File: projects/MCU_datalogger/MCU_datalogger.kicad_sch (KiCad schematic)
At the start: 25 parts, among them U1 24LC1025, U2 DS1337S_, U3 24LC1025, U4 ATMEGA328P-AU, Y1 32.768KHz, Y2 16MHz

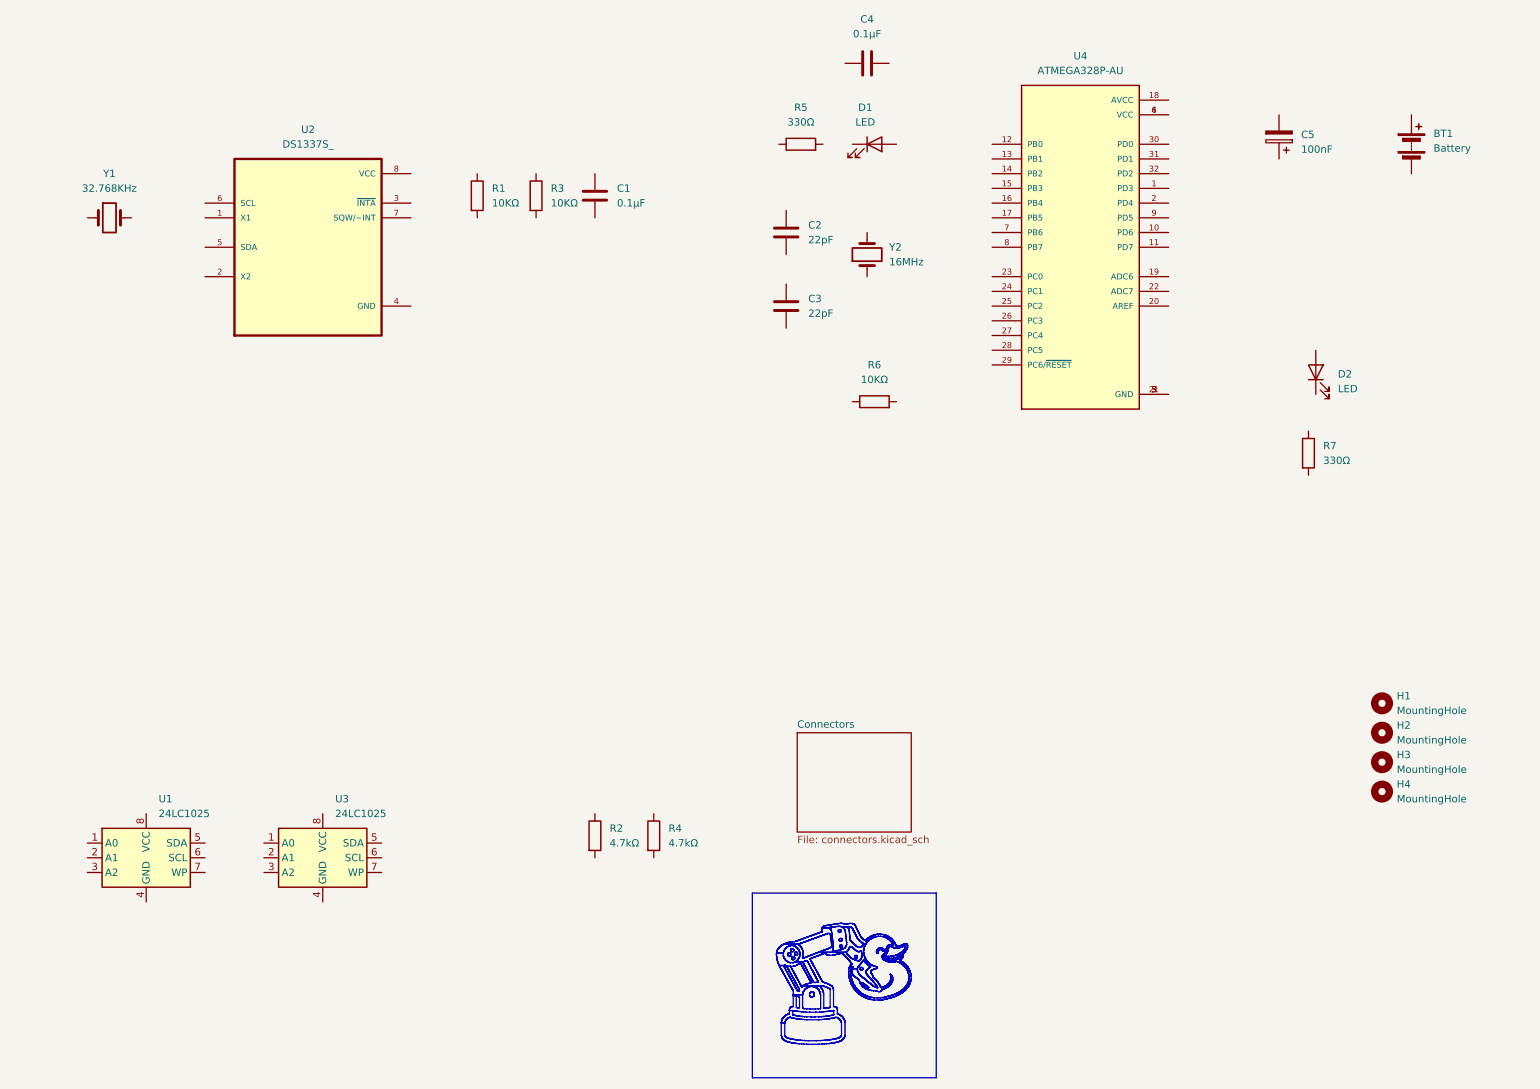
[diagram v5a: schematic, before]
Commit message: MCU datalogger - wiring of main sheet
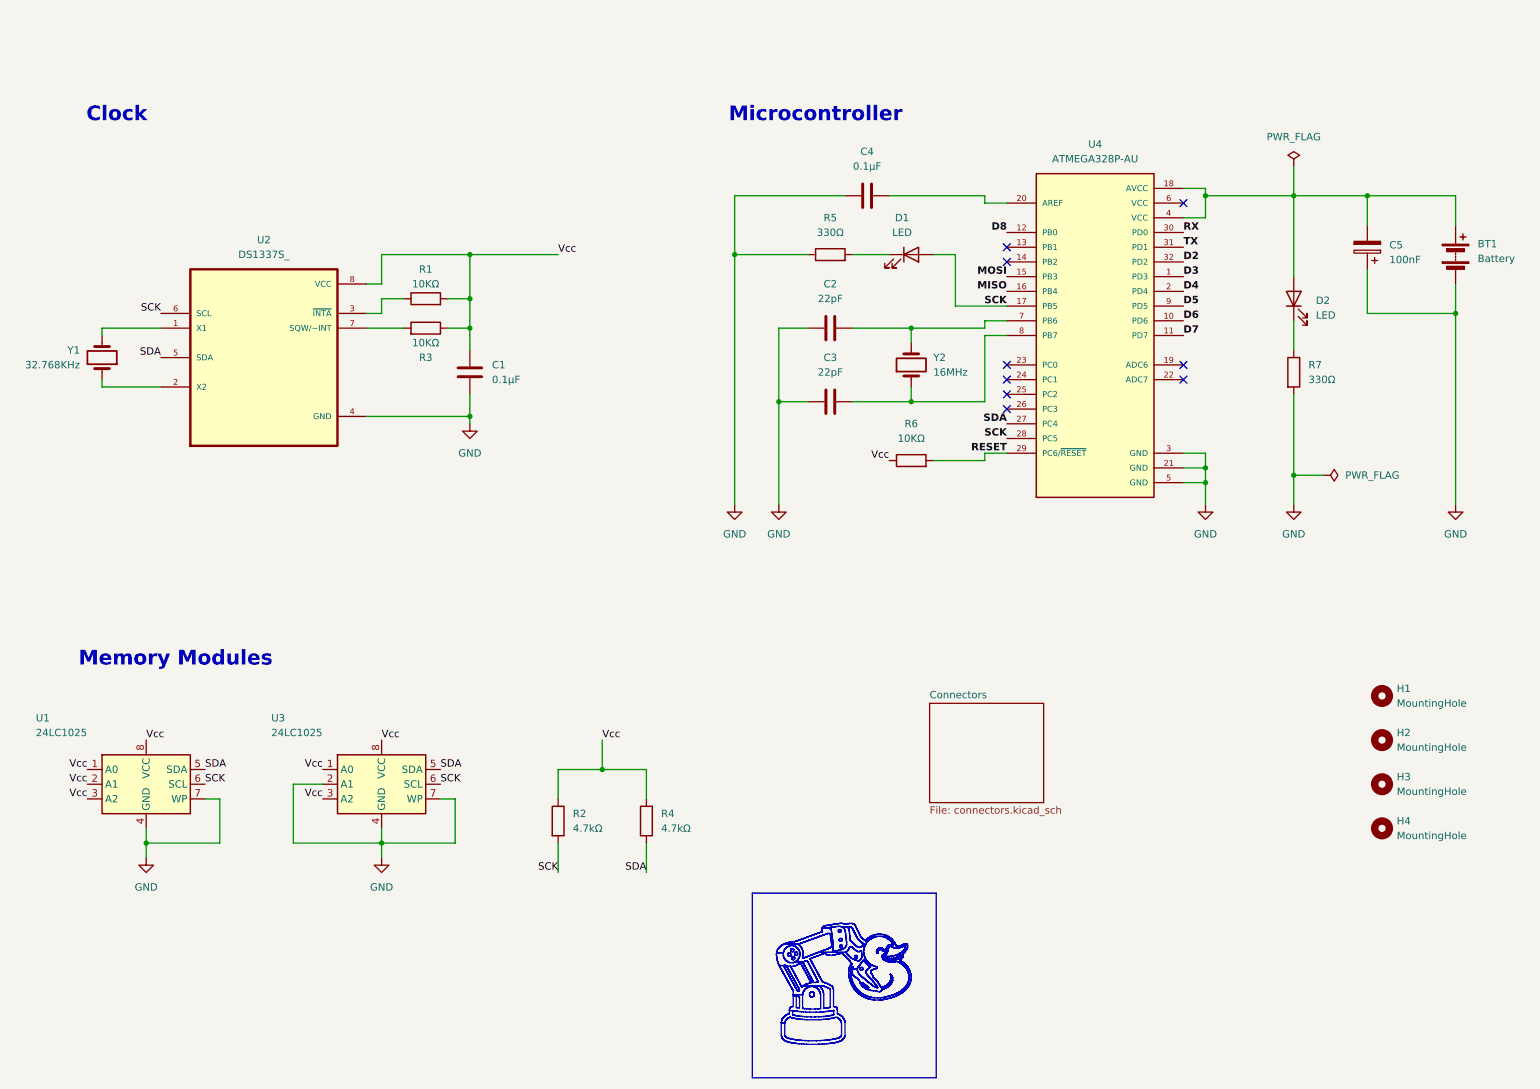
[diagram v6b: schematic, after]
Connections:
- net GND: now reaches C3.1
- net GND: now also BT1.2 (-), C1.2, C2.1, C4.1, C5.1, R5.1, R7.2, U1.4 (GND), U1.7 (WP), U2.4 (GND), U3.2 (A1), U3.4 (GND), U3.7 (WP), U4.21 (GND), U4.3 (GND), U4.5 (GND)
- net at C3.2: now also U4.8 (PB7), Y2.1
- net at BT1.1 (+): now also C5.2, D2.2 (A), U4.18 (AVCC), U4.4 (VCC)
- net at D2.1 (K): now also R7.1
- net Vcc: now reaches R4.1
- net Vcc: now also C1.1, R1.2, R2.1, R3.1, R6.1, U1.1 (A0), U1.2 (A1), U1.3 (A2), U1.8 (VCC), U2.8 (VCC), U3.1 (A0), U3.3 (A2), U3.8 (VCC)
- net SDA: now reaches R4.2
- net SDA: now also U1.5 (SDA), U2.5 (SDA), U3.5 (SDA), U4.27 (PC4)
- net at R5.2: now also D1.1 (K)
- net at C2.2: now also U4.7 (PB6), Y2.2
- net SCK: now reaches D1.2 (A)
- net SCK: now also R2.2, U1.6 (SCL), U2.6 (SCL), U3.6 (SCL), U4.17 (PB5), U4.28 (PC5)
- net at R3.2: now also U2.7 (SQW/~INT)
- net RESET: now reaches R6.2
- net RESET: now also U4.29 (PC6/~{RESET})
- net at Y1.1: now also U2.2 (X2)
- net at Y1.2: now also U2.1 (X1)
- net at C4.2: now also U4.20 (AREF)
- net at U2.3 (~{INTA}): now also R1.1
- net D3: now reaches U4.1 (PD3)
- net D6: now reaches U4.10 (PD6)
- net D7: now reaches U4.11 (PD7)
- net D8: now reaches U4.12 (PB0)
- net MOSI: now reaches U4.15 (PB3)
- net MISO: now reaches U4.16 (PB4)
- net D4: now reaches U4.2 (PD4)
- net RX: now reaches U4.30 (PD0)
- net TX: now reaches U4.31 (PD1)
- net D2: now reaches U4.32 (PD2)
- net at U4.6 (VCC): no longer U4.4 (VCC)
- net D5: now reaches U4.9 (PD5)
- no-connect marks 0 -> 9
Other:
- note added: "Clock"
- note added: "Memory Modules"
- note added: "Microcontroller"
- moved on the sheet: BT1, C1, C2, C3, C4, C5, D1, D2, H1, H2, H3, H4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

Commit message: MCU datalogger - wiring of second sheet
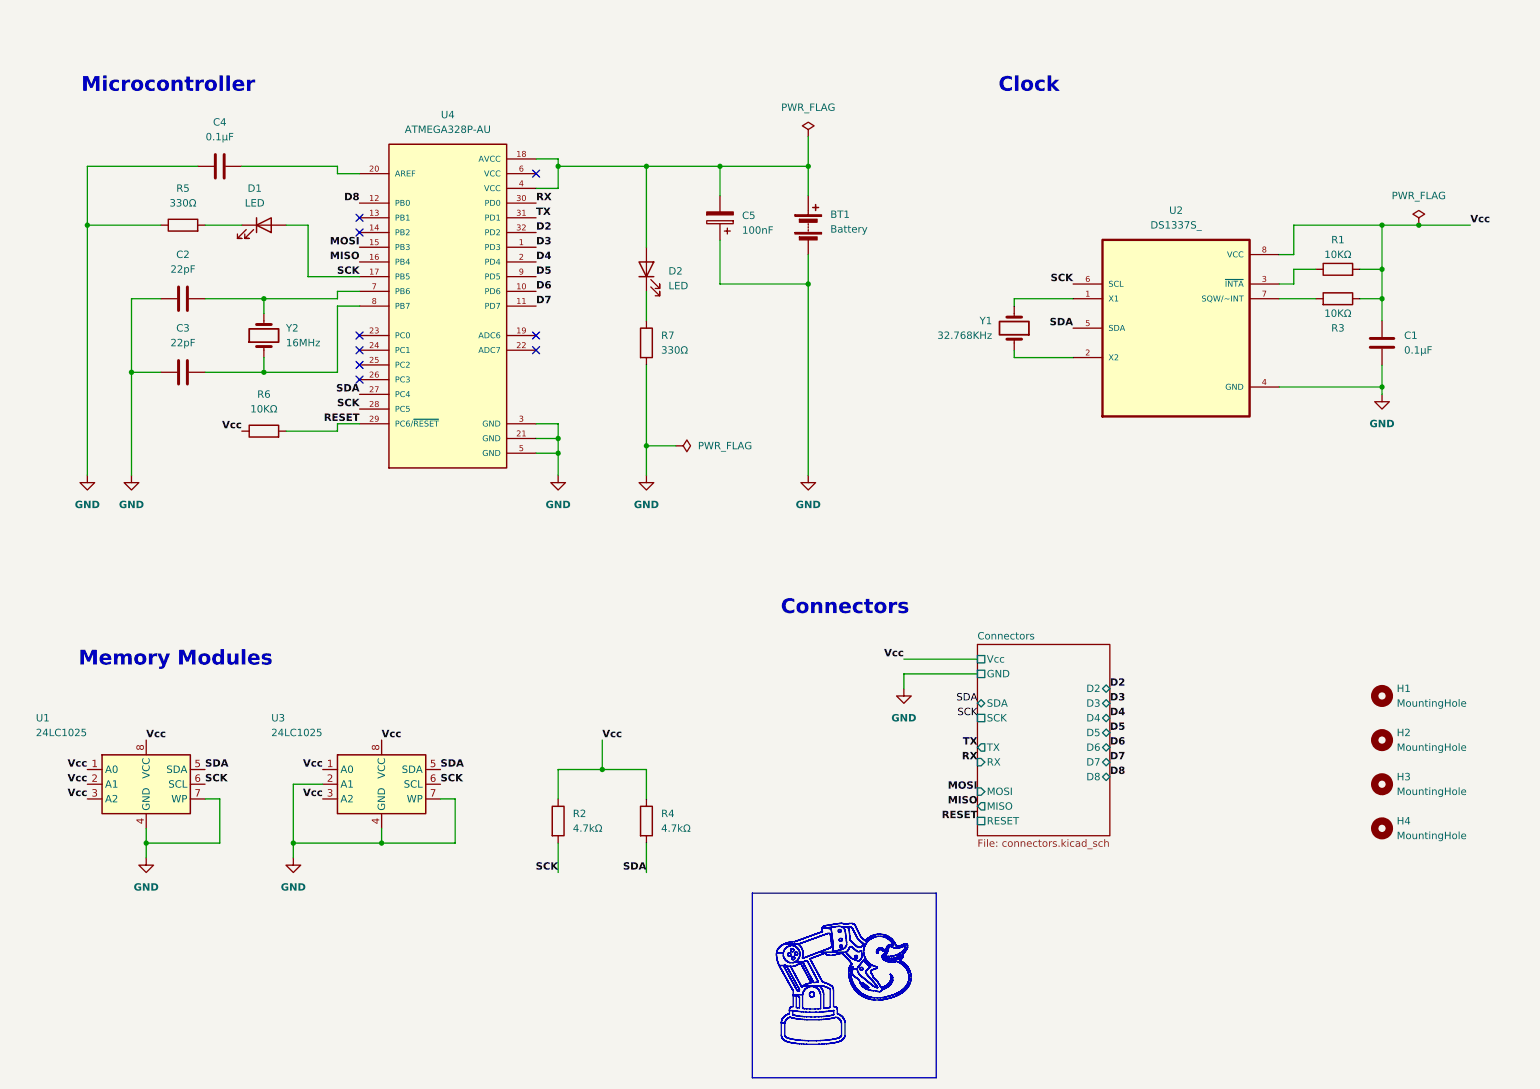
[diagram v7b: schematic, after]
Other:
- sheet Connectors ports: added D2, D3, D4, D5, D6, D7, D8, GND, MISO, MOSI, RESET, RX, SCK, SDA, TX, Vcc; removed none
- note added: "Connectors"
- moved on the sheet: BT1, C1, C2, C3, C4, C5, D1, D2, R1, R3, R5, R6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

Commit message: MCU datalogger - Assign nets GND and /Vcc to net class POWER, fix ERC warnings
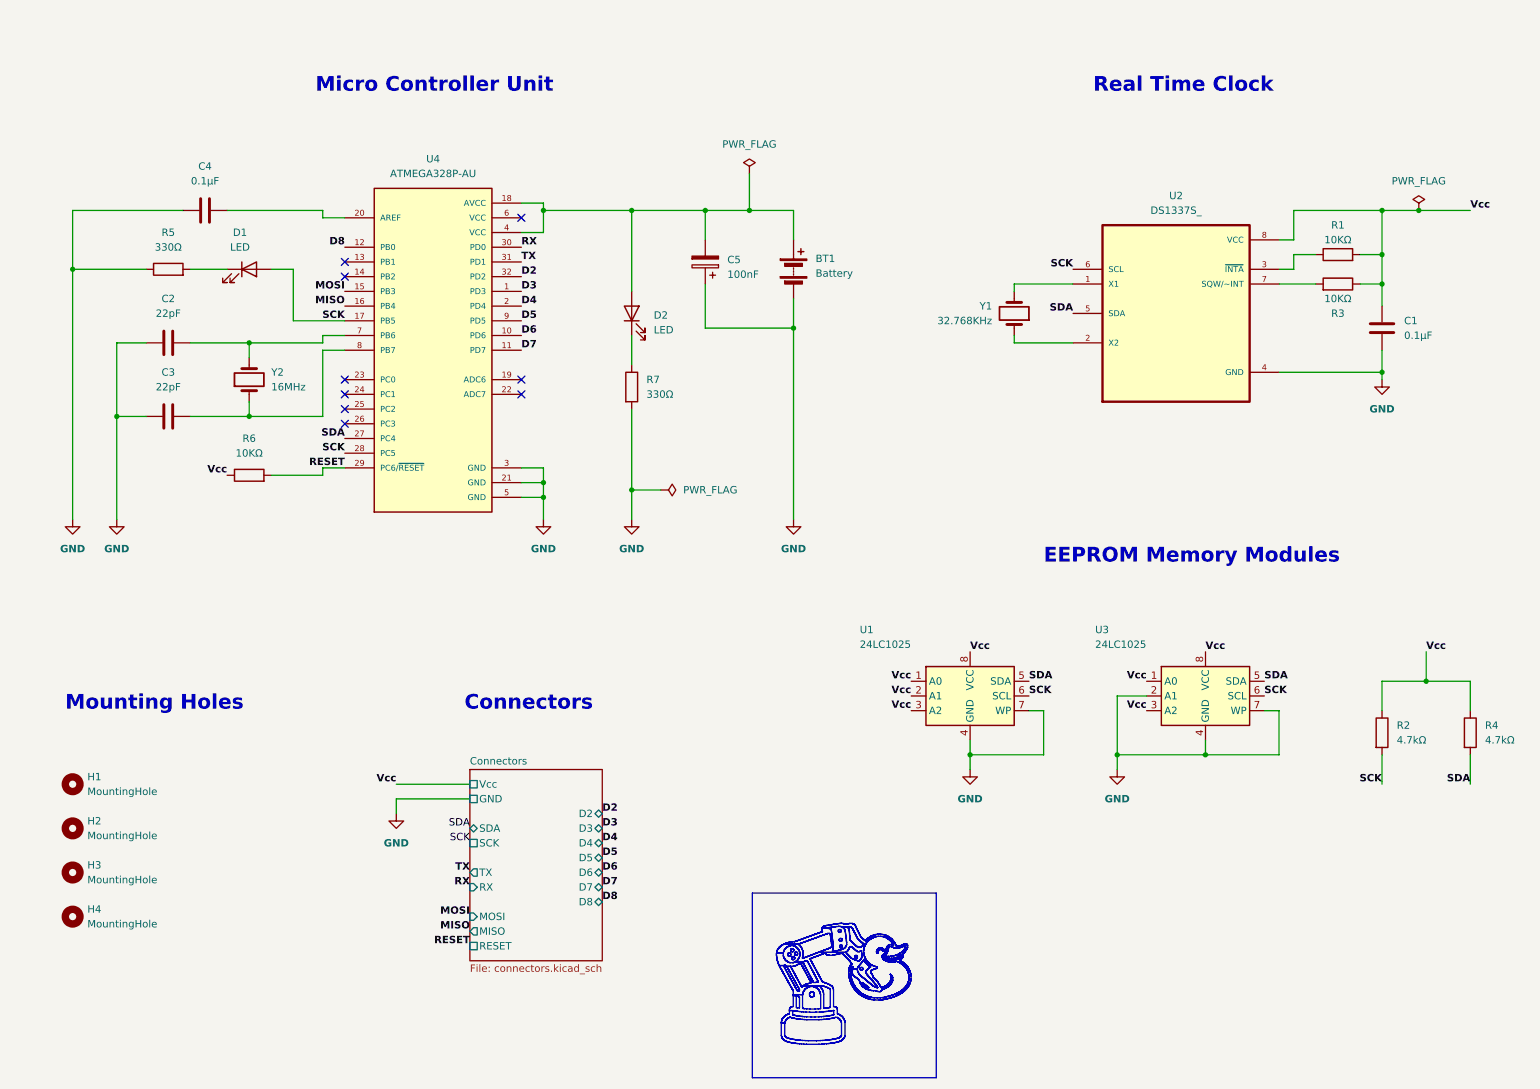
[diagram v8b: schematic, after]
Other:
- note added: "EEPROM Memory Modules"
- note added: "Micro Controller Unit"
- note added: "Mounting Holes"
- note added: "Real Time Clock"
- note removed: "Clock"
- note removed: "Memory Modules"
- note removed: "Microcontroller"
- moved on the sheet: BT1, C1, C2, C3, C4, C5, D1, D2, H1, H2, H3, H4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
